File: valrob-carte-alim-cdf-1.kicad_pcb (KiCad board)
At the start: 4 copper layers, 87 x 57 mm, 201 parts, among them J1 USB_C_Receptacle_USB2.0_14P, J10 Conn_01x02, J11 Conn_01x02, J12 Conn_01x02, J13 Conn_01x02, J14 Conn_01x02, J15 Conn_01x02, J16 Conn_01x02, J17 Conn_01x02, J18 Conn_01x02, J19 Conn_01x02, J2 Conn_01x02, J20 Conn_01x02, J21 Conn_01x02, J22 Conn_01x02, J3 Conn_01x04_Pin, J4 Conn_01x02, J5 Conn_01x02, J6 Conn_01x02, J7 Conn_01x02, J8 Conn_01x02, J9 Conn_01x02, SW1 SW_Push, SW2 SW_Push, SW3 SW_Push, U1 SN65HVD230, U10 TPS259472A, U11 TPS259472A, U12 TPS259472A, U2 ESP32-S3-WROOM-1, U3 TLV75733PDBV, U4 TPS56A37, U5 TPS56A37, U6 TPS259472A, U7 TPS259472A, U8 TPS259472A, U9 TPS259472A

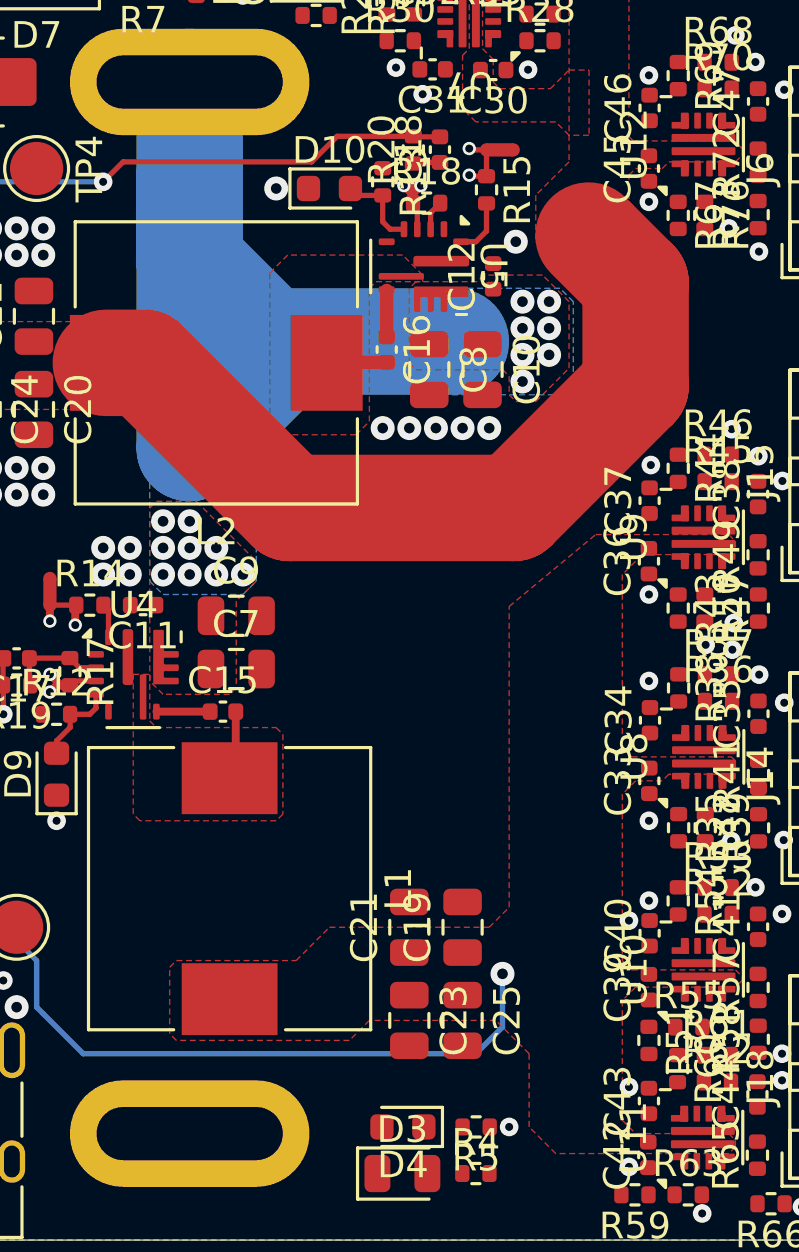
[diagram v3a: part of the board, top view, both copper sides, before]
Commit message: pcb: complete smps routing
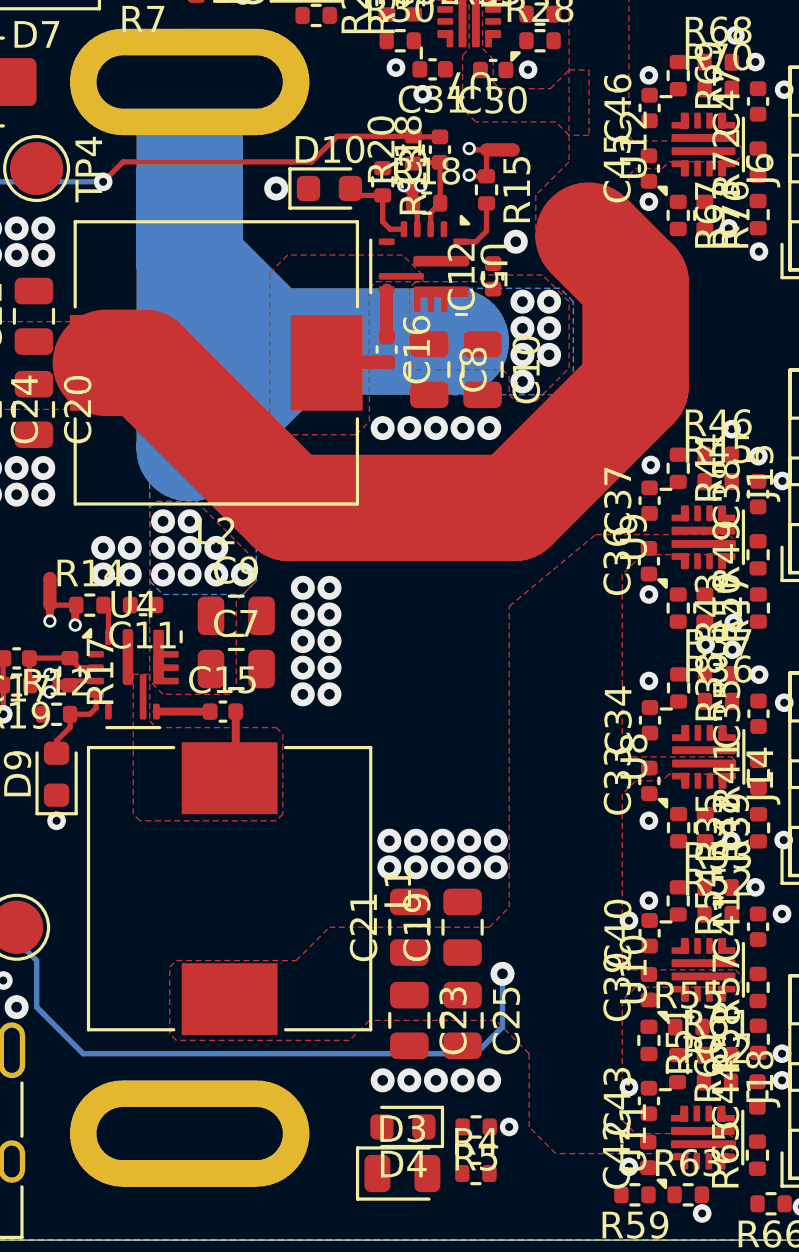
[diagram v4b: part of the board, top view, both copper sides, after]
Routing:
- net Net-(U5-FB): track 2.15 -> 3.68 mm
- net GND: vias 109 -> 134
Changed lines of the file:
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@@
+	)
+	(via
+		(at 130.75 86.5)
+		(size 0.9)
+		(drill 0.4)
+		(layers "F.Cu" "B.Cu")
+		(free yes)
+		(net 1)
+	)
+	(via
+		(at 130.75 85.5)
+		(size 0.9)
+		(drill 0.4)
+		(layers "F.Cu" "B.Cu")
+		(free yes)
+		(net 1)
 	)
 	(via
@@
 	)
 	(via
+		(at 136.75 104)
+		(size 0.9)
+		(drill 0.4)
+		(layers "F.Cu" "B.Cu")
+		(free yes)
+		(net 1)
+	)
+	(via
 		(at 128.75 70.5)
 		(size 0.9)
@@
 	)
 	(via
+		(at 129.75 88.5)
+		(size 0.9)
+		(drill 0.4)
+		(layers "F.Cu" "B.Cu")
+		(free yes)
+		(net 1)
+	)
+	(via
 		(at 119 82)
 		(size 0.9)
@@
 	)
 	(via
+		(at 137 95)
+		(size 0.9)
+		(drill 0.4)
+		(layers "F.Cu" "B.Cu")
+		(free yes)
+		(net 1)
+	)
+	(via
 		(at 104.5 97.25)
 		(size 0.9)
@@
 	)
 	(via
+		(at 133 96)
+		(size 0.9)
+		(drill 0.4)
+		(layers "F.Cu" "B.Cu")
+		(free yes)
+		(net 1)
+	)
+	(via
+		(at 129.75 87.5)
+		(size 0.9)
+		(drill 0.4)
+		(layers "F.Cu" "B.Cu")
+		(free yes)
+		(net 1)
+	)
+	(via
+		(at 136 95)
+		(size 0.9)
+		(drill 0.4)
+		(layers "F.Cu" "B.Cu")
+		(free yes)
+		(net 1)
+	)
+	(via
+		(at 134 95)
+		(size 0.9)
+		(drill 0.4)
+		(layers "F.Cu" "B.Cu")
+		(free yes)
+		(net 1)
+	)
+	(via
 		(at 111.25 100.25)
 		(size 0.7)
@@
 	)
 	(via
+		(at 134 96)
+		(size 0.9)
+		(drill 0.4)
+		(layers "F.Cu" "B.Cu")
+		(free yes)
+		(net 1)
+	)
+	(via
 		(at 128.25 62.5)
 		(size 0.7)
@@
 	)
 	(via
+		(at 134.75 104)
+		(size 0.9)
+		(drill 0.4)
+		(layers "F.Cu" "B.Cu")
+		(free yes)
+		(net 1)
+	)
+	(via
 		(at 142 107.25)
 		(size 0.7)
@@
 	)
 	(via
+		(at 133.75 104)
+		(size 0.9)
+		(drill 0.4)
+		(layers "F.Cu" "B.Cu")
+		(free yes)
+		(net 1)
+	)
+	(via
 		(at 132.75 79.5)
 		(size 0.9)
@@
 	)
 	(via
+		(at 132.75 104)
+		(size 0.9)
+		(drill 0.4)
+		(layers "F.Cu" "B.Cu")
+		(free yes)
+		(net 1)
+	)
+	(via
 		(at 118 82)
 		(size 0.9)
@@
 	)
 	(via
+		(at 136 96)
+		(size 0.9)
+		(drill 0.4)
+		(layers "F.Cu" "B.Cu")
+		(free yes)
+		(net 1)
+	)
+	(via
+		(at 129.75 86.5)
+		(size 0.9)
+		(drill 0.4)
+		(layers "F.Cu" "B.Cu")
+		(free yes)
+		(net 1)
+	)
+	(via
 		(at 117 82)
 		(size 0.9)
@@
 	)
 	(via
+		(at 137 96)
+		(size 0.9)
+		(drill 0.4)
+		(layers "F.Cu" "B.Cu")
+		(free yes)
+		(net 1)
+	)
+	(via
 		(at 91 94.5)
 		(size 0.9)
@@
 	)
 	(via
+		(at 130.75 89.5)
+		(size 0.9)
+		(drill 0.4)
+		(layers "F.Cu" "B.Cu")
+		(free yes)
+		(net 1)
+	)
+	(via
+		(at 135.75 104)
+		(size 0.9)
+		(drill 0.4)
+		(layers "F.Cu" "B.Cu")
+		(free yes)
+		(net 1)
+	)
+	(via
 		(at 113.5 68)
 		(size 0.9)
@@
 	)
 	(via
+		(at 130.75 87.5)
+		(size 0.9)
+		(drill 0.4)
+		(layers "F.Cu" "B.Cu")
+		(free yes)
+		(net 1)
+	)
+	(via
 		(at 123.25 84)
 		(size 0.9)
@@
 	)
 	(via
+		(at 129.75 85.5)
+		(size 0.9)
+		(drill 0.4)
+		(layers "F.Cu" "B.Cu")
+		(free yes)
+		(net 1)
+	)
+	(via
 		(at 142 104.25)
 		(size 0.7)
@@
 	)
 	(via
+		(at 130.75 88.5)
+		(size 0.9)
+		(drill 0.4)
+		(layers "F.Cu" "B.Cu")
+		(free yes)
+		(net 1)
+	)
+	(via
 		(at 133.75 79.5)
 		(size 0.9)
@@
 	)
 	(via
+		(at 135 95)
+		(size 0.9)
+		(drill 0.4)
+		(layers "F.Cu" "B.Cu")
+		(free yes)
+		(net 1)
+	)
+	(via
 		(at 137.75 72.5)
 		(size 0.9)
@@
 	)
 	(via
+		(at 129.75 89.5)
+		(size 0.9)
+		(drill 0.4)
+		(layers "F.Cu" "B.Cu")
+		(free yes)
+		(net 1)
+	)
+	(via
 		(at 117 73)
 		(size 0.9)
@@
 	)
 	(via
+		(at 135 96)
+		(size 0.9)
+		(drill 0.4)
+		(layers "F.Cu" "B.Cu")
+		(free yes)
+		(net 1)
+	)
+	(via
 		(at 134.25 66.96)
 		(size 0.7)
@@
 		(size 0.7)
 		(drill 0.3)
+		(layers "F.Cu" "B.Cu")
+		(free yes)
+		(net 1)
+	)
+	(via
+		(at 133 95)
+		(size 0.9)
+		(drill 0.4)
 		(layers "F.Cu" "B.Cu")
 		(free yes)
@@
 		(width 0.2)
 		(layer "F.Cu")
+		(net 13)
+	)
+	(segment
+		(start 134.91 71.05)
+		(end 134.91 69.53)
+		(width 0.2)
+		(layer "F.Cu")
+		(net 13)
+	)
+	(segment
+		(start 134.91 69.53)
+		(end 134.9 69.52)
+		(width 0.2)
+		(layer "F.Cu")

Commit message: pcb: add efuse 5v 3 routing
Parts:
- moved R28 36.3 mm to (103.0, 71.8)
- moved R75 0.55 mm to (138.7, 64.5)
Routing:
- net /Connectors/Efuse 5V 5A 3/OUT: track 0.00 -> 22.1 mm
- net PG_5V_3: track 0.00 -> 10.1 mm, vias 0 -> 2
- net Net-(U7-PGTH): track 0.00 -> 2.46 mm
- net Net-(U7-DVDT): track 0.00 -> 1.45 mm
- net Net-(U7-OVCSEL): track 0.00 -> 1.36 mm
- net Net-(U7-ITIMER): track 0.00 -> 1.33 mm
- net GND: track 0.00 -> 0.95 mm, vias 134 -> 135
- added copper zone on F.Cu, net /Connectors/Efuse 5V 5A 3/OUT

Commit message: pcb: add esp and ldo 3v3 routing
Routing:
- net +5V: track 58.0 -> 106.5 mm, vias 2 -> 4
- net +3V3: track 1.81 -> 22.1 mm
- net Net-(D2-K): track 0.00 -> 6.59 mm
- net Net-(D12-A): track 0.00 -> 1.68 mm

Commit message: schem: reorganize programmable gpios
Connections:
- U2 pad 11: EN_5V_1 -> PG_12V_3
- U2 pad 12: PG_5V_2 -> EN_12V_3
- U2 pad 15: ILM_12V_4 -> ILM_5V_2
- U2 pad 17: /Vsense -> /PG_12V
- U2 pad 18: PG_12V_3 -> PG_12V_1
- U2 pad 19: PG_5V_3 -> EN_12V_1
- U2 pad 21: PG_12V_1 -> EN_12V_2
- U2 pad 23: EN_12V_3 -> PG_5V_2
- U2 pad 24: EN_12V_2 -> EN_5V_2
- U2 pad 25: EN_12V_1 -> /Vsense
- U2 pad 30: /BAU -> /PG_5V
- U2 pad 31: EN_5V_3 -> PG_5V_1
- U2 pad 32: Net-(D3-K) -> EN_5V_1
- U2 pad 33: PG_5V_1 -> EN_5V_3
- U2 pad 34: /PG_5V -> PG_5V_3
- U2 pad 35: /PG_12V -> /BAU
- U2 pad 38: ILM_5V_2 -> ILM_5V_3
- U2 pad 4: ILM_5V_3 -> ILM_12V_4
- U2 pad 5: ILM_12V_1 -> ILM_12V_3
- U2 pad 6: ILM_12V_2 -> ILM_12V_1
- U2 pad 7: ILM_12V_3 -> ILM_12V_2
- U2 pad 8: EN_5V_2 -> unconnected-(U2-GPIO15/U0RTS/ADC2_CH4/XTAL_32K_P-Pad8)
- U2 pad 9: unconnected-(U2-GPIO16/U0CTS/ADC2_CH5/XTAL_32K_N-Pad9) -> Net-(D3-K)
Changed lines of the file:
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@@
 	(net 92 "unconnected-(U1-Vref-Pad5)")
 	(net 93 "unconnected-(U2-GPIO45-Pad26)")
-	(net 94 "unconnected-(U2-GPIO14{slash}TOUCH14{slash}ADC2_CH3{slash}FSPIWP{slash}FSPIDQS{slash}SUBSPIWP-Pad22)")
-	(net 95 "unconnected-(U2-GPIO46-Pad16)")
-	(net 96 "unconnected-(U2-GPIO16{slash}U0CTS{slash}ADC2_CH5{slash}XTAL_32K_N-Pad9)")
-	(net 97 "unconnected-(U3-NC-Pad4)")
-	(net 98 "unconnected-(U4-SS-Pad5)")
-	(net 99 "unconnected-(U4-EN-Pad1)")
-	(net 100 "unconnected-(U5-SS-Pad5)")
-	(net 101 "unconnected-(U5-EN-Pad1)")
-	(net 102 "Net-(U6-OVCSEL)")
-	(net 103 "Net-(U7-OVCSEL)")
-	(net 104 "Net-(U12-OVCSEL)")
+	(net 94 "unconnected-(U2-GPIO46-Pad16)")
+	(net 95 "unconnected-(U3-NC-Pad4)")
+	(net 96 "unconnected-(U4-SS-Pad5)")
+	(net 97 "unconnected-(U4-EN-Pad1)")
+	(net 98 "unconnected-(U5-SS-Pad5)")
+	(net 99 "unconnected-(U5-EN-Pad1)")
+	(net 100 "Net-(U6-OVCSEL)")
+	(net 101 "Net-(U7-OVCSEL)")
+	(net 102 "Net-(U12-OVCSEL)")
+	(net 103 "unconnected-(U2-GPIO15{slash}U0RTS{slash}ADC2_CH4{slash}XTAL_32K_P-Pad8)")
+	(net 104 "unconnected-(U2-GPIO14{slash}TOUCH14{slash}ADC2_CH3{slash}FSPIWP{slash}FSPIDQS{slash}SUBSPIWP-Pad22)")
 	(footprint "LED_SMD:LED_0805_2012Metric"
 		(layer "F.Cu")
@@
 			(layers "F.Cu" "F.Mask" "F.Paste")
 			(roundrect_rratio 0.15)
-			(net 102 "Net-(U6-OVCSEL)")
+			(net 100 "Net-(U6-OVCSEL)")
 			(pinfunction "OVCSEL")
 			(pintype "input")
@@
 			(layers "F.Cu" "F.Mask" "F.Paste")
 			(roundrect_rratio 0.25)
-			(net 101 "unconnected-(U5-EN-Pad1)")
+			(net 99 "unconnected-(U5-EN-Pad1)")
 			(pinfunction "EN")
 			(pintype "input+no_connect")
@@
 			(layers "F.Cu" "F.Mask" "F.Paste")
 			(roundrect_rratio 0.25)
-			(net 100 "unconnected-(U5-SS-Pad5)")
+			(net 98 "unconnected-(U5-SS-Pad5)")
 			(pinfunction "SS")
 			(pintype "input+no_connect")
@@
 			(layers "F.Cu" "F.Mask" "F.Paste")
 			(roundrect_rratio 0.25)
-			(net 104 "Net-(U12-OVCSEL)")
+			(net 102 "Net-(U12-OVCSEL)")
 			(pintype "passive")
 		)
@@
 			(layers "F.Cu" "F.Mask" "F.Paste")
 			(roundrect_rratio 0.15)
-			(net 103 "Net-(U7-OVCSEL)")
+			(net 101 "Net-(U7-OVCSEL)")
 			(pinfunction "OVCSEL")
 			(pintype "input")
@@
 			(layers "F.Cu" "F.Mask" "F.Paste")
 			(roundrect_rratio 0.25)
-			(net 102 "Net-(U6-OVCSEL)")
+			(net 100 "Net-(U6-OVCSEL)")
 			(pintype "passive")
 		)
@@
 			(layers "F.Cu" "F.Mask" "F.Paste")
 			(roundrect_rratio 0.25)
-			(net 97 "unconnected-(U3-NC-Pad4)")
+			(net 95 "unconnected-(U3-NC-Pad4)")
 			(pinfunction "NC")
 			(pintype "no_connect")
@@
 			(layers "F.Cu" "F.Mask" "F.Paste")
 			(roundrect_rratio 0.25)
-			(net 99 "unconnected-(U4-EN-Pad1)")
+			(net 97 "unconnected-(U4-EN-Pad1)")
 			(pinfunction "EN")
 			(pintype "input+no_connect")
@@
 			(layers "F.Cu" "F.Mask" "F.Paste")
 			(roundrect_rratio 0.25)
-			(net 98 "unconnected-(U4-SS-Pad5)")
+			(net 96 "unconnected-(U4-SS-Pad5)")
 			(pinfunction "SS")
 			(pintype "input+no_connect")
@@
 			(size 1.5 0.9)
 			(layers "F.Cu" "F.Mask" "F.Paste")
-			(net 73 "ILM_5V_3")
+			(net 84 "ILM_12V_4")
 			(pinfunction "GPIO4/TOUCH4/ADC1_CH3")
 			(pintype "bidirectional")
@@
 			(size 1.5 0.9)
 			(layers "F.Cu" "F.Mask" "F.Paste")
-			(net 75 "ILM_12V_1")
+			(net 81 "ILM_12V_3")
 			(pinfunction "GPIO5/TOUCH5/ADC1_CH4")
 			(pintype "bidirectional")
@@
 			(size 1.5 0.9)
 			(layers "F.Cu" "F.Mask" "F.Paste")
-			(net 78 "ILM_12V_2")
+			(net 75 "ILM_12V_1")
 			(pinfunction "GPIO6/TOUCH6/ADC1_CH5")
 			(pintype "bidirectional")
@@
 			(size 1.5 0.9)
 			(layers "F.Cu" "F.Mask" "F.Paste")
-			(net 81 "ILM_12V_3")
+			(net 78 "ILM_12V_2")
 			(pinfunction "GPIO7/TOUCH7/ADC1_CH6")
 			(pintype "bidirectional")
@@
 			(size 1.5 0.9)
 			(layers "F.Cu" "F.Mask" "F.Paste")
-			(net 63 "EN_5V_2")
+			(net 103 "unconnected-(U2-GPIO15{slash}U0RTS{slash}ADC2_CH4{slash}XTAL_32K_P-Pad8)")
 			(pinfunction "GPIO15/U0RTS/ADC2_CH4/XTAL_32K_P")
-			(pintype "bidirectional")
+			(pintype "bidirectional+no_connect")
 		)
 		(pad "9" smd rect
@@
 			(size 1.5 0.9)
 			(layers "F.Cu" "F.Mask" "F.Paste")
-			(net 96 "unconnected-(U2-GPIO16{slash}U0CTS{slash}ADC2_CH5{slash}XTAL_32K_N-Pad9)")
+			(net 30 "Net-(D3-K)")
 			(pinfunction "GPIO16/U0CTS/ADC2_CH5/XTAL_32K_N")
-			(pintype "bidirectional+no_connect")
+			(pintype "bidirectional")
 		)
 		(pad "10" smd rect
@@
 			(size 1.5 0.9)
 			(layers "F.Cu" "F.Mask" "F.Paste")
-			(net 58 "EN_5V_1")
+			(net 42 "PG_12V_3")
 			(pinfunction "GPIO18/U1RXD/ADC2_CH7/CLK_OUT3")
 			(pintype "bidirectional")
@@
 			(size 1.5 0.9)
 			(layers "F.Cu" "F.Mask" "F.Paste")
-			(net 44 "PG_5V_2")
+			(net 62 "EN_12V_3")
 			(pinfunction "GPIO8/TOUCH8/ADC1_CH7/SUBSPICS1")
 			(pintype "bidirectional")
@@
 			(size 1.5 0.9)
 			(layers "F.Cu" "F.Mask" "F.Paste")
-			(net 84 "ILM_12V_4")
+			(net 87 "ILM_5V_2")
 			(pinfunction "GPIO3/TOUCH3/ADC1_CH2")
 			(pintype "bidirectional")
@@
 			(size 1.5 0.9)
 			(layers "F.Cu" "F.Mask" "F.Paste")
-			(net 95 "unconnected-(U2-GPIO46-Pad16)")
+			(net 94 "unconnected-(U2-GPIO46-Pad16)")
 			(pinfunction "GPIO46")
 			(pintype "bidirectional+no_connect")
@@
 			(size 1.5 0.9)
 			(layers "F.Cu" "F.Mask" "F.Paste")
-			(net 6 "/Vsense")
+			(net 35 "/PG_12V")
 			(pinfunction "GPIO9/TOUCH9/ADC1_CH8/FSPIHD/SUBSPIHD")
 			(pintype "bidirectional")
@@
 			(size 1.5 0.9)
 			(layers "F.Cu" "F.Mask" "F.Paste")
-			(net 42 "PG_12V_3")
+			(net 40 "PG_12V_1")
 			(pinfunction "GPIO10/TOUCH10/ADC1_CH9/FSPICS0/FSPIIO4/SUBSPICS0")
 			(pintype "bidirectional")
@@
 			(size 1.5 0.9)
 			(layers "F.Cu" "F.Mask" "F.Paste")
-			(net 39 "PG_5V_3")
+			(net 60 "EN_12V_1")
 			(pinfunction "GPIO11/TOUCH11/ADC2_CH0/FSPID/FSPIIO5/SUBSPID")
 			(pintype "bidirectional")
@@
 			(size 1.5 0.9)
 			(layers "F.Cu" "F.Mask" "F.Paste")
-			(net 40 "PG_12V_1")
+			(net 61 "EN_12V_2")
 			(pinfunction "GPIO13/TOUCH13/ADC2_CH2/FSPIQ/FSPIIO7/SUBSPIQ")
 			(pintype "bidirectional")
@@
 			(size 1.5 0.9)
 			(layers "F.Cu" "F.Mask" "F.Paste")
-			(net 94 "unconnected-(U2-GPIO14{slash}TOUCH14{slash}ADC2_CH3{slash}FSPIWP{slash}FSPIDQS{slash}SUBSPIWP-Pad22)")
+			(net 104 "unconnected-(U2-GPIO14{slash}TOUCH14{slash}ADC2_CH3{slash}FSPIWP{slash}FSPIDQS{slash}SUBSPIWP-Pad22)")
 			(pinfunction "GPIO14/TOUCH14/ADC2_CH3/FSPIWP/FSPIDQS/SUBSPIWP")
 			(pintype "bidirectional+no_connect")
@@
 			(size 1.5 0.9)
 			(layers "F.Cu" "F.Mask" "F.Paste")
-			(net 62 "EN_12V_3")
+			(net 44 "PG_5V_2")
 			(pinfunction "GPIO21")
 			(pintype "bidirectional")
@@
 			(size 1.5 0.9)
 			(layers "F.Cu" "F.Mask" "F.Paste")
-			(net 61 "EN_12V_2")
+			(net 63 "EN_5V_2")
 			(pinfunction "GPIO47/SPICLK_P/SUBSPICLK_P_DIFF")
 			(pintype "bidirectional")
@@
 			(size 1.5 0.9)
 			(layers "F.Cu" "F.Mask" "F.Paste")
-			(net 60 "EN_12V_1")
+			(net 6 "/Vsense")
 			(pinfunction "GPIO48/SPICLK_N/SUBSPICLK_N_DIFF")
 			(pintype "bidirectional")
@@
 			(size 1.5 0.9)
 			(layers "F.Cu" "F.Mask" "F.Paste")
-			(net 89 "/BAU")
+			(net 36 "/PG_5V")
 			(pinfunction "SPIDQS/GPIO37/FSPIQ/SUBSPIQ")
 			(pintype "bidirectional")
@@
 			(size 1.5 0.9)
 			(layers "F.Cu" "F.Mask" "F.Paste")
-			(net 59 "EN_5V_3")
+			(net 38 "PG_5V_1")
 			(pinfunction "GPIO38/FSPIWP/SUBSPIWP")
 			(pintype "bidirectional")
@@
 			(size 1.5 0.9)
 			(layers "F.Cu" "F.Mask" "F.Paste")
-			(net 30 "Net-(D3-K)")
+			(net 58 "EN_5V_1")
 			(pinfunction "MTCK/GPIO39/CLK_OUT3/SUBSPICS1")
 			(pintype "bidirectional")
@@
 			(size 1.5 0.9)
 			(layers "F.Cu" "F.Mask" "F.Paste")
-			(net 38 "PG_5V_1")
+			(net 59 "EN_5V_3")
 			(pinfunction "MTDO/GPIO40/CLK_OUT2")
 			(pintype "bidirectional")
@@
 			(size 1.5 0.9)
 			(layers "F.Cu" "F.Mask" "F.Paste")
-			(net 36 "/PG_5V")
+			(net 39 "PG_5V_3")
 			(pinfunction "MTDI/GPIO41/CLK_OUT1")
 			(pintype "bidirectional")
@@
 			(size 1.5 0.9)
 			(layers "F.Cu" "F.Mask" "F.Paste")
-			(net 35 "/PG_12V")
+			(net 89 "/BAU")
 			(pinfunction "MTMS/GPIO42")
 			(pintype "bidirectional")
@@
 			(size 1.5 0.9)
 			(layers "F.Cu" "F.Mask" "F.Paste")
-			(net 87 "ILM_5V_2")
+			(net 73 "ILM_5V_3")
 			(pinfunction "GPIO2/TOUCH2/ADC1_CH1")
 			(pintype "bidirectional")
@@
 			(layers "F.Cu" "F.Mask" "F.Paste")
 			(roundrect_rratio 0.15)
-			(net 104 "Net-(U12-OVCSEL)")
+			(net 102 "Net-(U12-OVCSEL)")
 			(pinfunction "OVCSEL")
 			(pintype "input")
@@
 			(layers "F.Cu" "F.Mask" "F.Paste")
 			(roundrect_rratio 0.25)
-			(net 103 "Net-(U7-OVCSEL)")
+			(net 101 "Net-(U7-OVCSEL)")
 			(pintype "passive")
 		)
@@
 		(width 0.2)
 		(layer "F.Cu")
-		(net 103)
+		(net 101)
 	)
 	(segment
@@
 		(width 0.2)
 		(layer "F.Cu")
-		(net 103)
+		(net 101)
 	)
 	(segment
@@
 		(width 0.2)
 		(layer "F.Cu")
-		(net 103)
+		(net 101)
 	)
 	(zone
